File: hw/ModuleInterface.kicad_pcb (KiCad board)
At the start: 2 copper layers, 48.3 x 99.1 mm, 56 parts, among them J1 clock, J10 out7, J11 out8, J12 interface_to_mid, J2 cv1, J3 cv2, J4 out1, J5 out2, J6 out3, J7 out4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

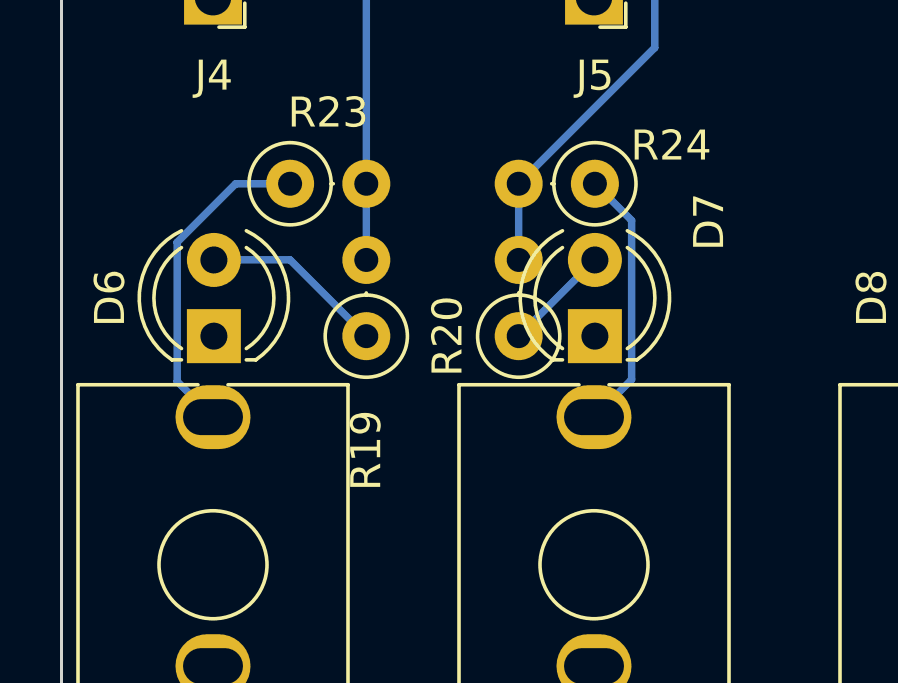
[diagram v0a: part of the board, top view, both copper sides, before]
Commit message: Software: - Added CV control, but for limited functions. - Added BPM mode.
Hardware:
- Version ordered to Elecrow.
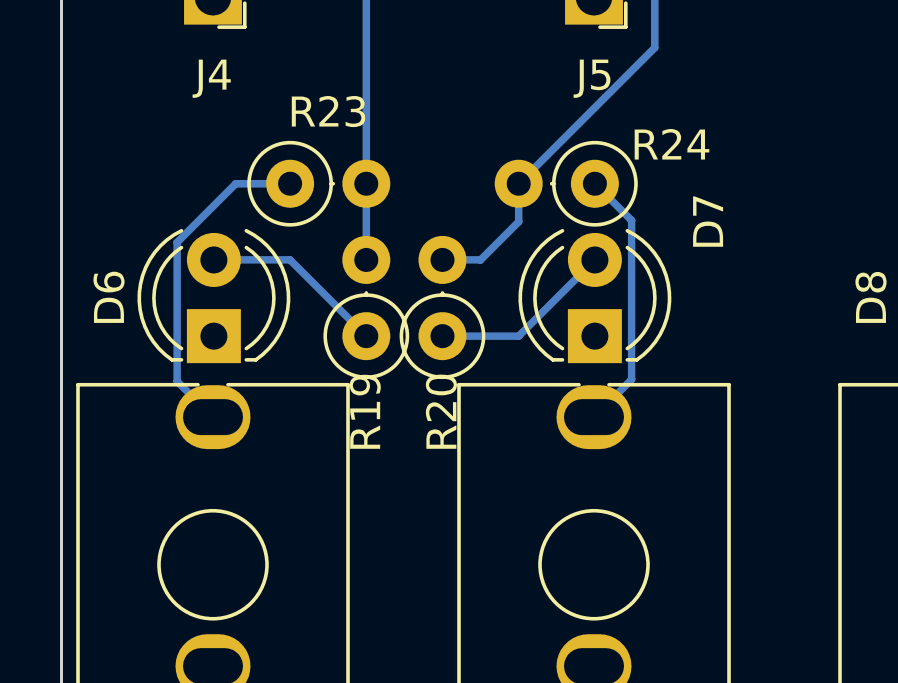
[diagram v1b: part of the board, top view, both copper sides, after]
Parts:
- moved R20 2.54 mm to (86.4, 129.5)
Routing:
- net Net-(D7-Pad2): track 3.59 -> 6.13 mm
- net /Interface/out_6: track 35.7 -> 37.5 mm
